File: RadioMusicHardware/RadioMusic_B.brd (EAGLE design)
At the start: 107 x 19.5 mm, 26 parts, among them U1 TEENSY_3.1_TW, U2 MCP6002, U3 TL072_

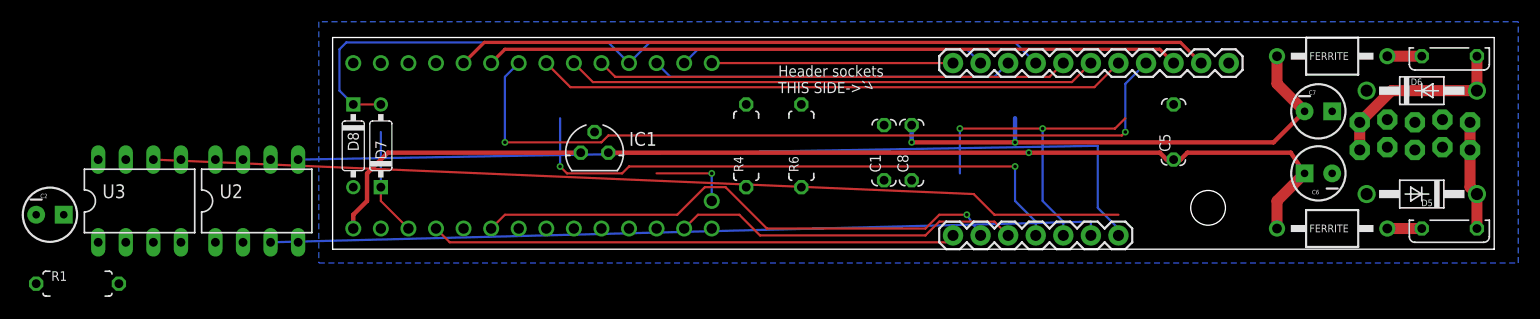
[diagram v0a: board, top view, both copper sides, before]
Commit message: starting SMD needs layout
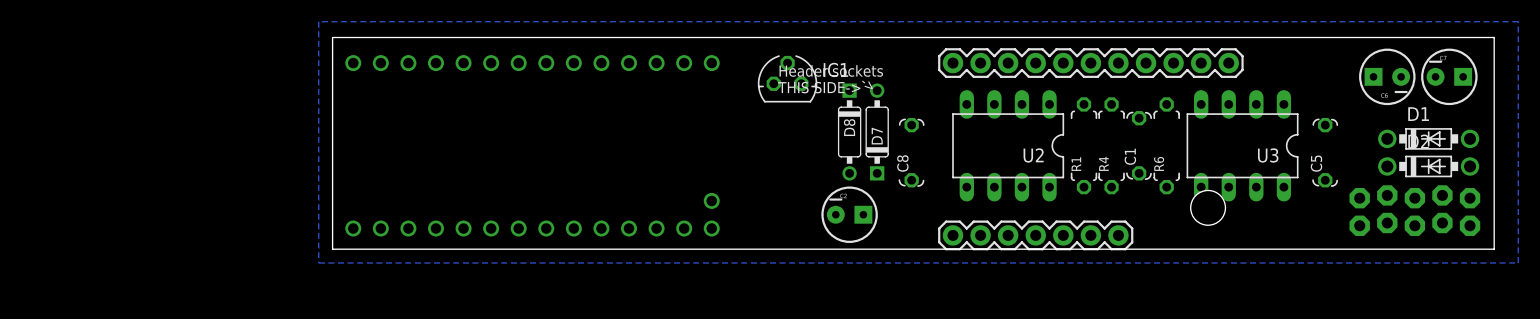
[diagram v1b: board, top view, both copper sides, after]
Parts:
- removed D5, D6: 1N4001, diode:DO41-10
- removed F1, F2: FUSE, TomW:C050H075X075
- removed L1, L2: BL01RN1A, inductors:BL01RN1A
- added D1, D2: 1N5819-B, diode:DO41-7.6
- moved U3 101.7 mm to (83.8, 9.53), turned to 180 degrees
- moved R1 93.6 mm to (69.2, 9.53), turned to 90 degrees
- moved C2 73.7 mm to (47.6, 3.17)
- moved U2 69.4 mm to (62.2, 9.53), turned to 180 degrees
- moved D7 45.7 mm to (50.2, 10.8)
- moved D8 45.7 mm to (47.6, 10.8)
- moved R4 33.7 mm to (71.8, 9.53)
- moved R6 33.7 mm to (76.8, 9.53)
- moved C1 23.5 mm to (74.3, 9.53)
- moved IC1 18.9 mm to (41.9, 15.2)
- moved C5 14.1 mm to (91.4, 8.89)
- moved C7 12.5 mm to (102.9, 15.9)
- moved C6 10.9 mm to (97.2, 15.9)
- moved SV1 6.99 mm to (99.7, 3.56)
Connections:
- removed net +12V_INLET: D5.C, F1.1, SV1.POS1, SV1.POS2
- removed net -12V_INLET: D6.A, F2.1, SV1.NEG1, SV1.NEG2
- removed net N$22: F1.2, L1.2
- removed net N$23: F2.2, L2.2
- new net N$2: D1.A, SV1.POS1, SV1.POS2
- new net N$6: D2.C, SV1.NEG1, SV1.NEG2
- net +12V: now also D1.C; no longer L1.1
- net -12V: now also D2.A; no longer L2.1
- net GND: no longer D5.A, D6.C
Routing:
- net N$7: track 89.8 -> 0.00 mm
- net TIME_CV: track 82.7 -> 0.00 mm
- net CHANNEL_CV: track 76.9 -> 0.00 mm
- net RESET_CV: track 74.9 -> 0.00 mm
- net LED3: track 72.5 -> 0.00 mm, vias 2 -> 0
- net +12V: track 71.8 -> 0.00 mm, vias 1 -> 0
- net LED1: track 69.5 -> 0.00 mm
- net +3.3V: track 64.0 -> 0.00 mm, vias 2 -> 0
- net LED2: track 63.9 -> 0.00 mm
- net LED4: track 54.5 -> 0.00 mm
- net TIME_POT: track 49.8 -> 0.00 mm, vias 1 -> 0
- net MOSI: track 49.1 -> 0.00 mm
- net CHANNEL_POT: track 48.4 -> 0.00 mm
- net -12V: track 47.3 -> 0.00 mm, vias 2 -> 0
- net RESET_SW: track 43.6 -> 0.00 mm
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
